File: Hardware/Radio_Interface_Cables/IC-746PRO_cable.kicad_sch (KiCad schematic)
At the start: 5 parts, among them J11 6.25 mm Plug, J12 3.5 mm Plug, J13 ACC(2), DIN-7, J21 ACC(1), DIN-8, J9 RJ45

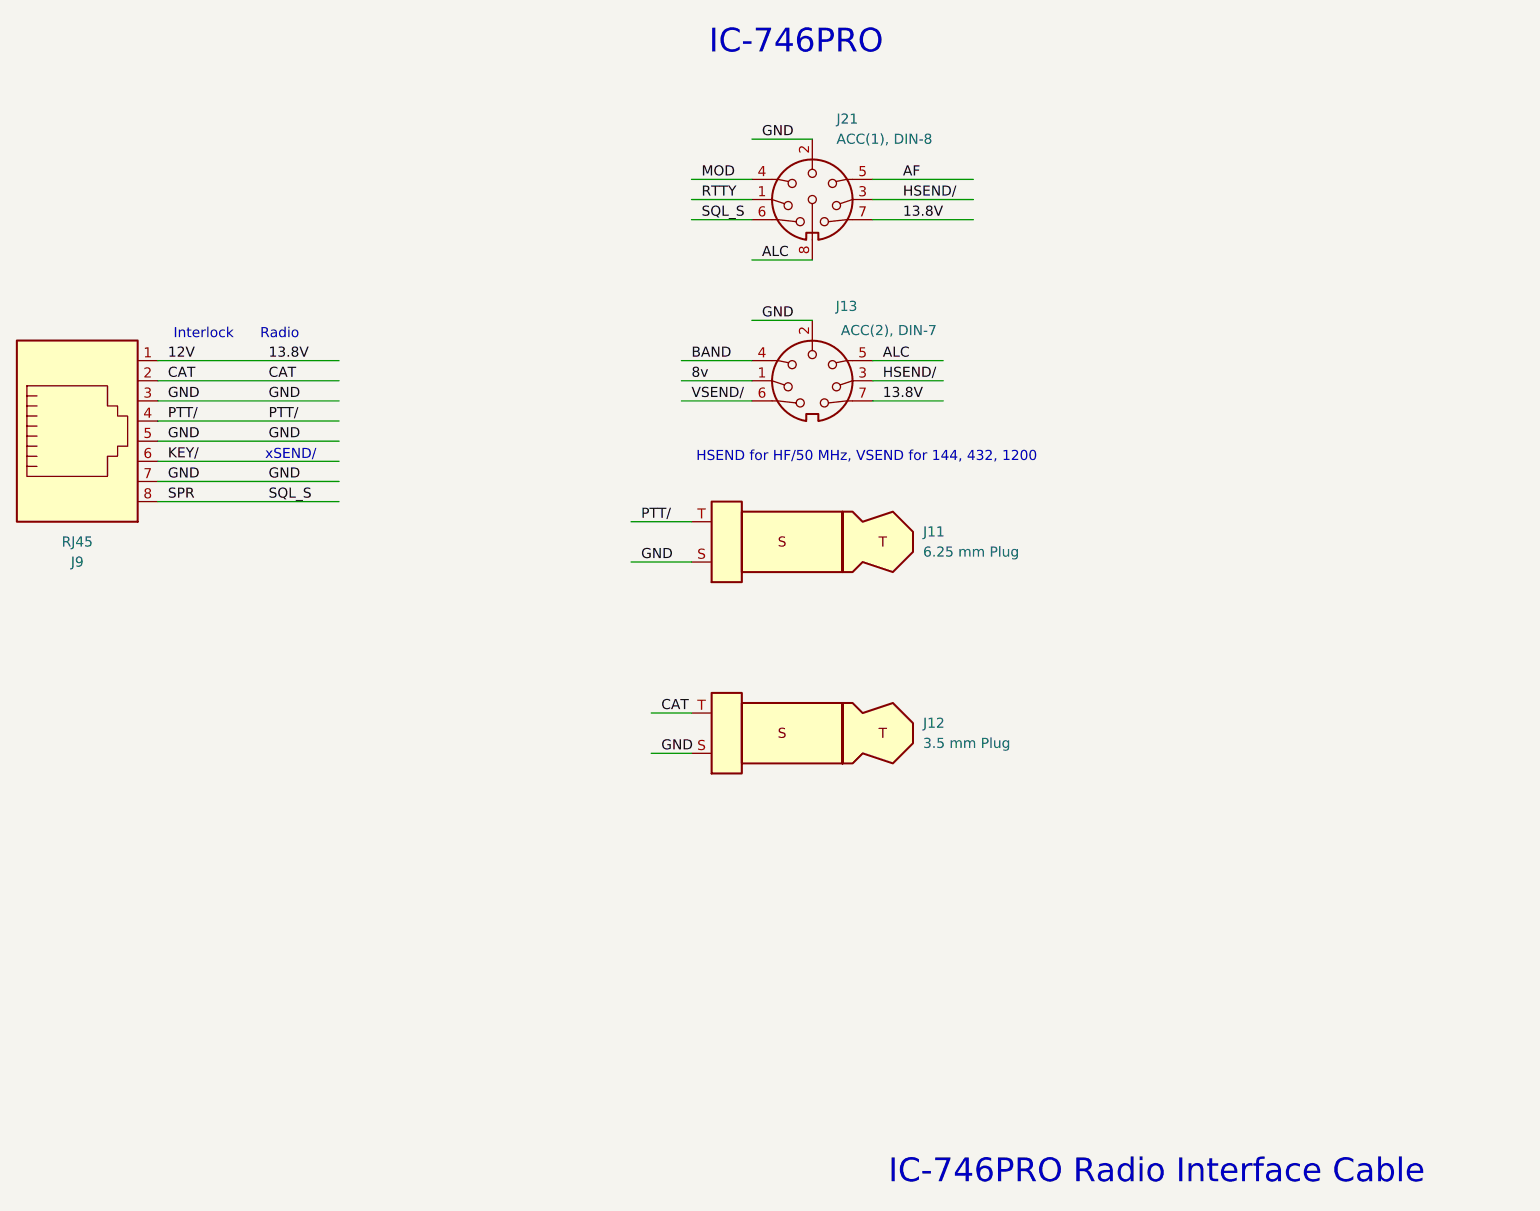
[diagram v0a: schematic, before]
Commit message: Add PTT and CAT connectors on Radio Interface Cables Mark pins as unused
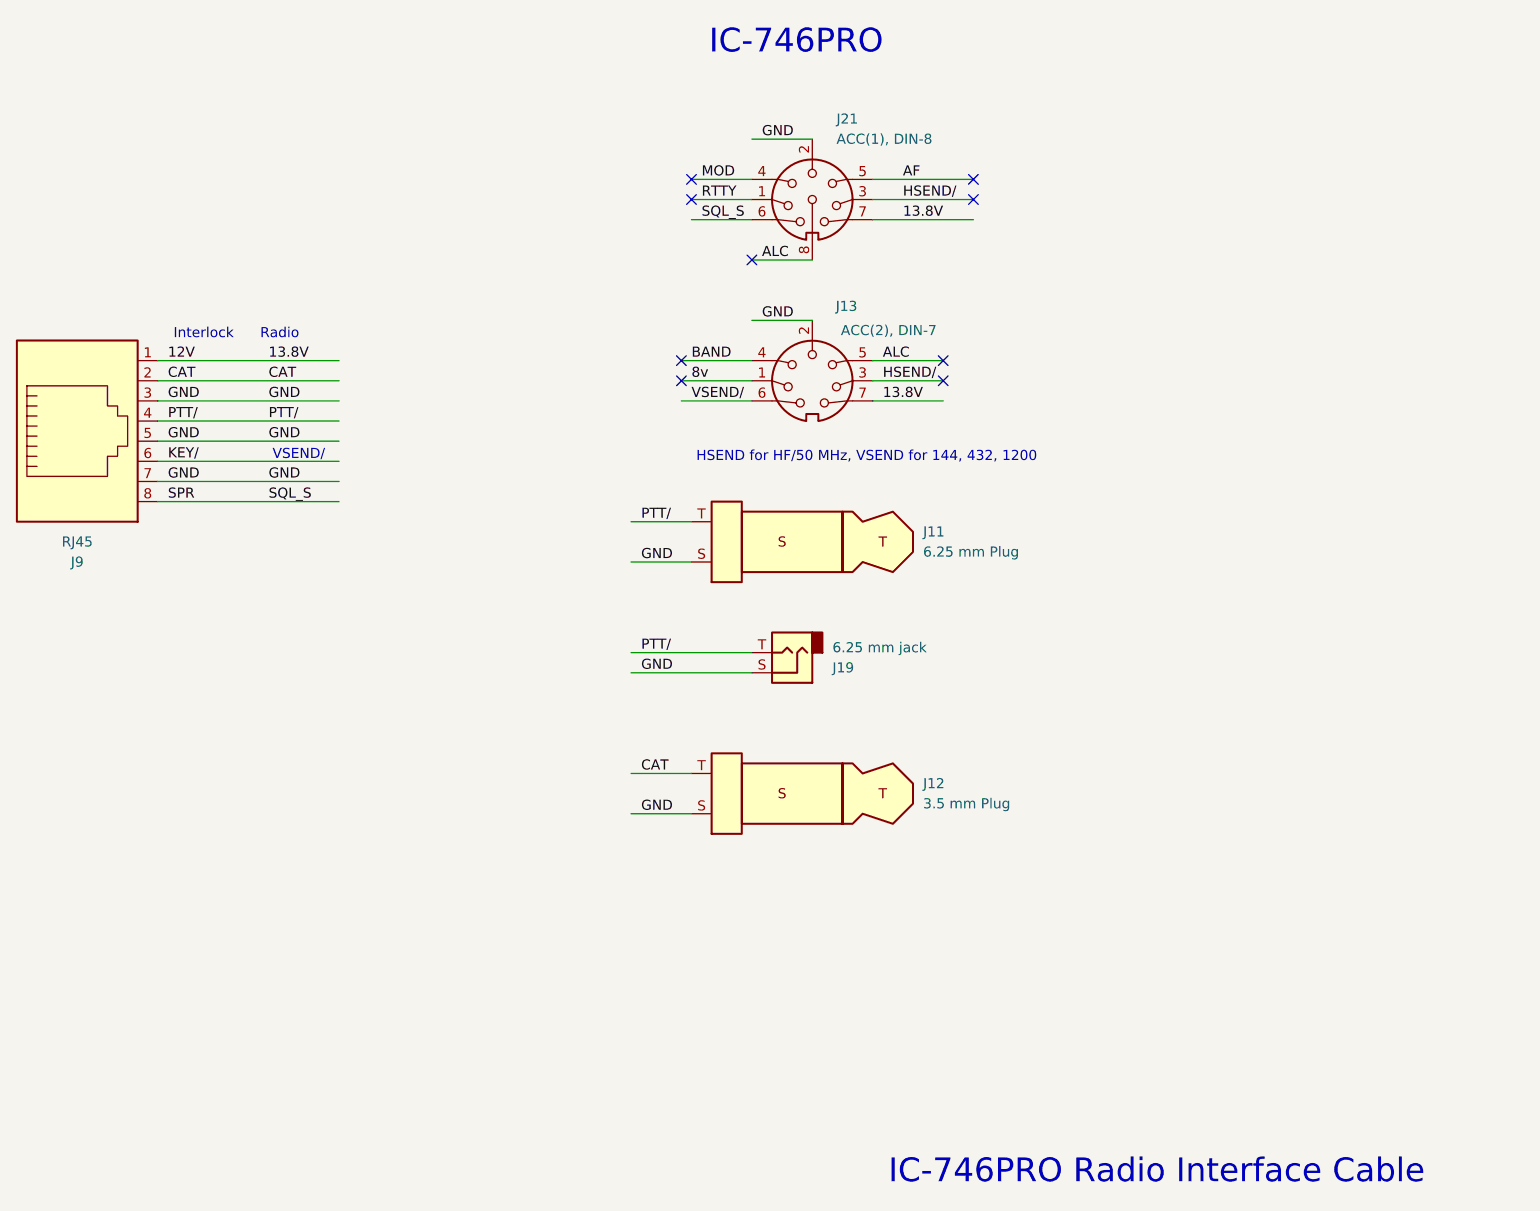
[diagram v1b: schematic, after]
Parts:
- added J19: 6.25 mm jack, symbol Connector_Audio:AudioJack2
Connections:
- net GND: now also J19.S
- net PTT/: now also J19.T
- no-connect marks 0 -> 9
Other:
- note added: "VSEND/"
- note removed: "xSEND/"
- moved on the sheet: J12
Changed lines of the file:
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@@
 		)
 	)
-	(text "xSEND/"
+	(text "VSEND/"
 		(exclude_from_sim no)
-		(at 112.014 83.058 0)
-		(effects
-			(font
-				(size 1.27 1.27)
-			)
-		)
+		(at 113.03 83.058 0)
+		(effects
+			(font
+				(size 1.27 1.27)
+			)
+		)
+	)
+	(no_connect
+		(at 161.29 73.66)
+	)
+	(no_connect
+		(at 198.12 48.26)
+	)
+	(no_connect
+		(at 194.31 73.66)
+	)
+	(no_connect
+		(at 161.29 71.12)
+	)
+	(no_connect
+		(at 198.12 50.8)
+	)
+	(no_connect
+		(at 170.18 58.42)
+	)
+	(no_connect
+		(at 162.56 50.8)
+	)
+	(no_connect
+		(at 194.31 71.12)
+	)
+	(no_connect
+		(at 162.56 48.26)
 	)
 	(wire
@@
 	(wire
 		(pts
-			(xy 157.48 115.57) (xy 162.56 115.57)
+			(xy 154.94 123.19) (xy 162.56 123.19)
+		)
+		(stroke
+			(width 0)
+			(type default)
+		)
+	)
+	(wire
+		(pts
+			(xy 154.94 110.49) (xy 170.18 110.49)
 		)
 		(stroke
@@
 	(wire
 		(pts
+			(xy 154.94 107.95) (xy 170.18 107.95)
+		)
+		(stroke
+			(width 0)
+			(type default)
+		)
+	)
+	(wire
+		(pts
 			(xy 161.29 73.66) (xy 170.18 73.66)
 		)
@@
 	(wire
 		(pts
-			(xy 157.48 120.65) (xy 162.56 120.65)
+			(xy 154.94 128.27) (xy 162.56 128.27)
 		)
 		(stroke
@@
 	)
 	(label "CAT"
-		(at 158.75 115.57 0)
+		(at 156.21 123.19 0)
 		(effects
 			(font
@@
 		)
 	)
+	(label "PTT{slash}"
+		(at 156.21 107.95 0)
+		(effects
+			(font
+				(size 1.27 1.27)
+			)
+			(justify left bottom)
+		)
+	)
 	(label "HSEND{slash}"
 		(at 186.69 73.66 0)
@@
 	)
 	(label "GND"
+		(at 156.21 110.49 0)
+		(effects
+			(font
+				(size 1.27 1.27)
+			)
+			(justify left bottom)
+		)
+	)
+	(label "GND"
 		(at 96.52 81.28 0)
 		(effects
@@
 	)
 	(label "GND"
-		(at 158.75 120.65 0)
-		(effects
-			(font
-				(size 1.27 1.27)
-			)
-			(justify left bottom)
+		(at 156.21 128.27 0)
+		(effects
+			(font
+				(size 1.27 1.27)
+			)
+			(justify left bottom)
+		)
+	)
+	(symbol
+		(lib_id "Connector_Audio:AudioJack2")
+		(at 175.26 107.95 180)
+		(unit 1)
+		(exclude_from_sim no)
+		(in_bom yes)
+		(on_board yes)
+		(dnp no)
+		(property "Reference" "J19"
+			(at 180.34 109.8551 0)
+			(effects
+				(font
+					(size 1.27 1.27)
+				)
+				(justify right)
+			)
+		)
+		(property "Value" "6.25 mm jack"
+			(at 180.34 107.3151 0)
+			(effects
+				(font
+					(size 1.27 1.27)
+				)
+				(justify right)
+			)
+		)
+		(property "Footprint" ""
+			(at 175.26 107.95 0)
+			(effects
+				(font
+					(size 1.27 1.27)
+				)
+				(hide yes)
+			)
+		)
+		(property "Datasheet" "~"
+			(at 175.26 107.95 0)
+			(effects
+				(font
+					(size 1.27 1.27)
+				)
+				(hide yes)
+			)
+		)
+		(property "Description" "Audio Jack, 2 Poles (Mono / TS)"
+			(at 175.26 107.95 0)
+			(effects
+				(font
+					(size 1.27 1.27)
+				)
+				(hide yes)
+			)
+		)
+		(pin "S"
+		)
+		(pin "T"
+		)
+		(instances
+			(project ""
+				(path "/65a6842f-7ce8-4a1d-bd27-c5cbbec442dc/fcfd43f8-6244-4e92-81b0-daf6ea50b53f"
+					(reference "J19")
+					(unit 1)
+				)
+			)
 		)
 	)
 	(symbol
 		(lib_id "Connector_Audio:AudioPlug2")
-		(at 177.8 118.11 180)
+		(at 177.8 125.73 180)
 		(unit 1)
 		(exclude_from_sim no)
@@
 		(fields_autoplaced yes)
 		(property "Reference" "J12"
-			(at 191.77 116.8399 0)
+			(at 191.77 124.4599 0)
 			(effects
 				(font
@@
 		)
 		(property "Value" "3.5 mm Plug"
-			(at 191.77 119.3799 0)
+			(at 191.77 126.9999 0)
 			(effects
 				(font
@@
 		)
 		(property "Footprint" ""
-			(at 168.91 116.84 0)
+			(at 168.91 124.46 0)
 			(effects
 				(font
@@
 		)
 		(property "Datasheet" "~"
-			(at 168.91 116.84 0)
+			(at 168.91 124.46 0)
 			(effects
 				(font
@@
 		)
 		(property "Description" "Audio Jack, 2 Poles (Mono / TS)"
-			(at 177.8 118.11 0)
+			(at 177.8 125.73 0)
 			(effects
 				(font
